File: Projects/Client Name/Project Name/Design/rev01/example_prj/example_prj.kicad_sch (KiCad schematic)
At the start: 0 parts

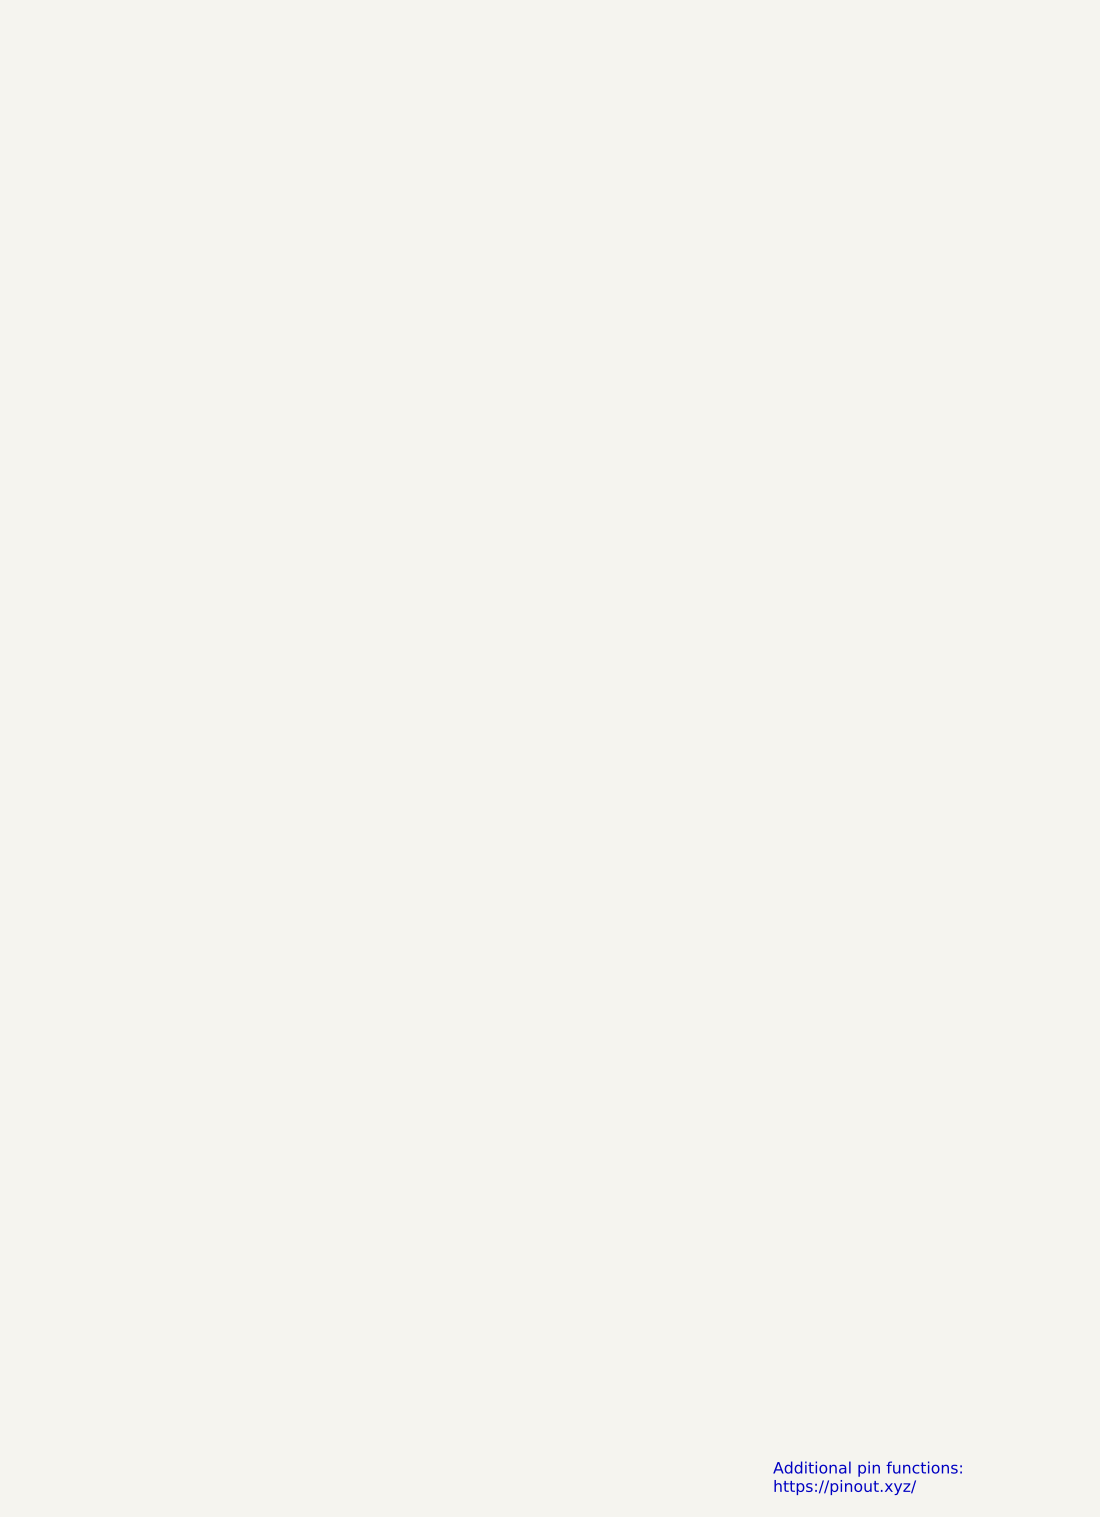
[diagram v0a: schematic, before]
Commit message: Block Diagram sch
Creation of block diagram schematic and general schematic page
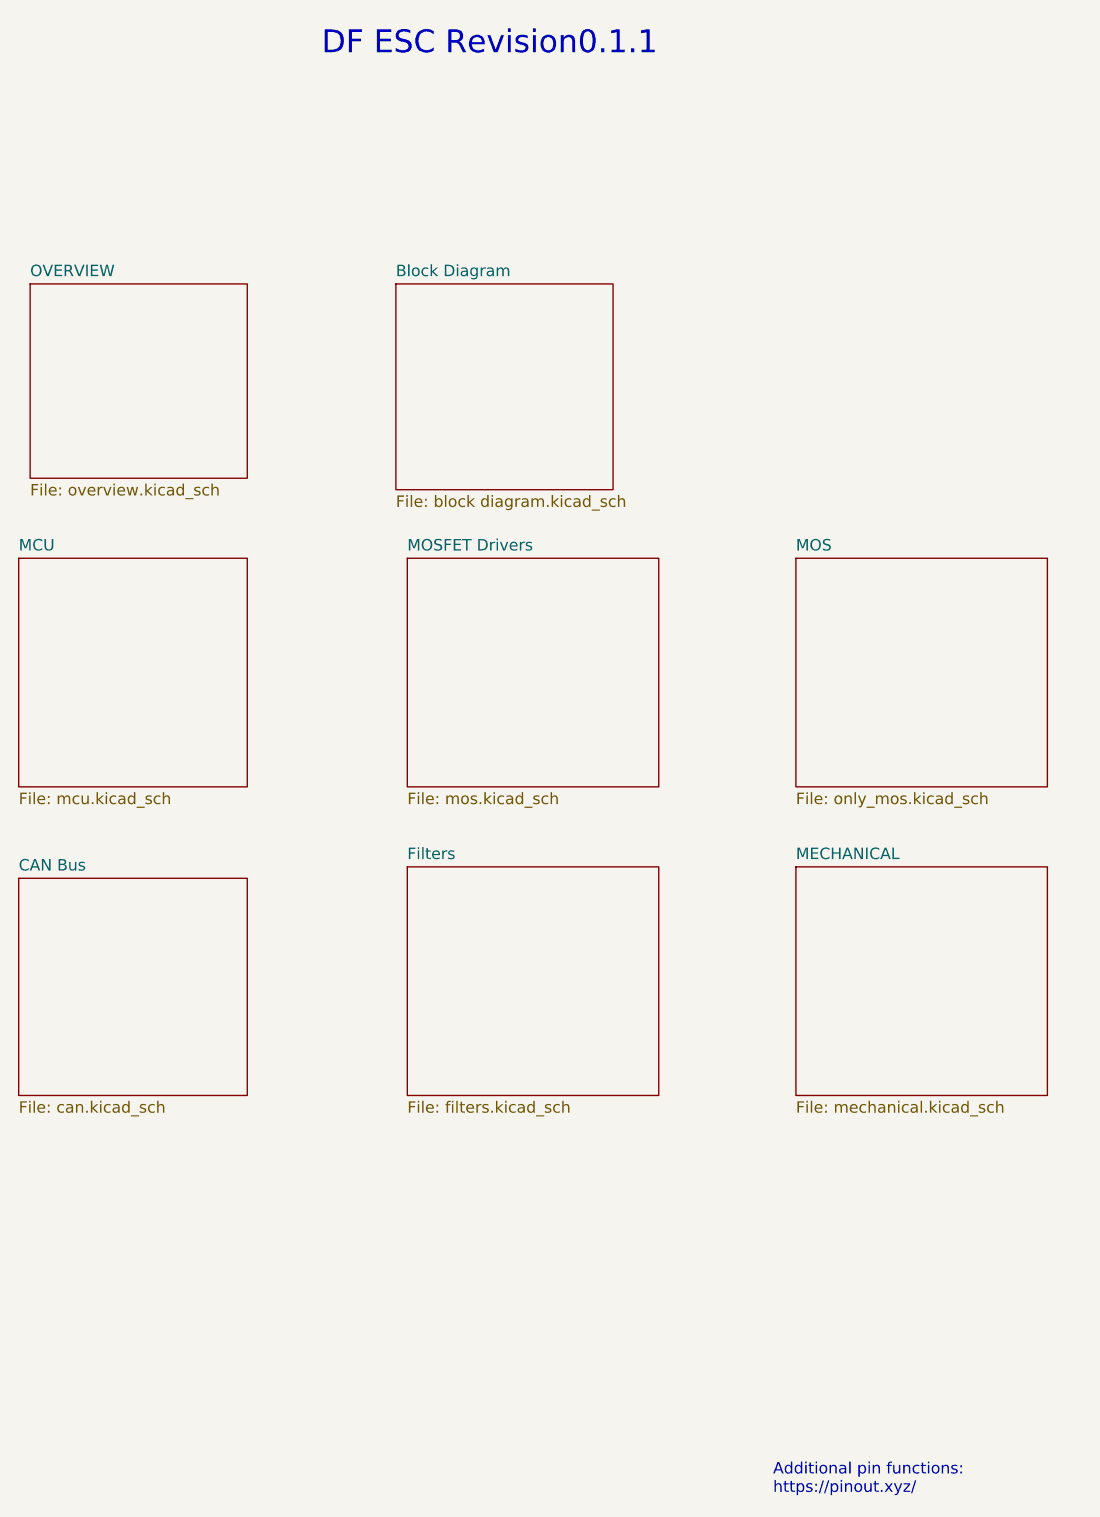
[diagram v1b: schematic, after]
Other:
- added sheet Block Diagram (block diagram.kicad_sch)
- added sheet CAN Bus (can.kicad_sch)
- added sheet Filters (filters.kicad_sch)
- added sheet MCU (mcu.kicad_sch)
- added sheet MECHANICAL (mechanical.kicad_sch)
- added sheet MOS (only_mos.kicad_sch)
- added sheet MOSFET Drivers (mos.kicad_sch)
- added sheet OVERVIEW (overview.kicad_sch)
- note added: "DF ESC Revision0.1.1"
- title: (none) -> ESC
